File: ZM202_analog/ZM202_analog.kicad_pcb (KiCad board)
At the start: 2 copper layers, 3 parts, among them U1 2N4416, U2 TL431, U3 LM324

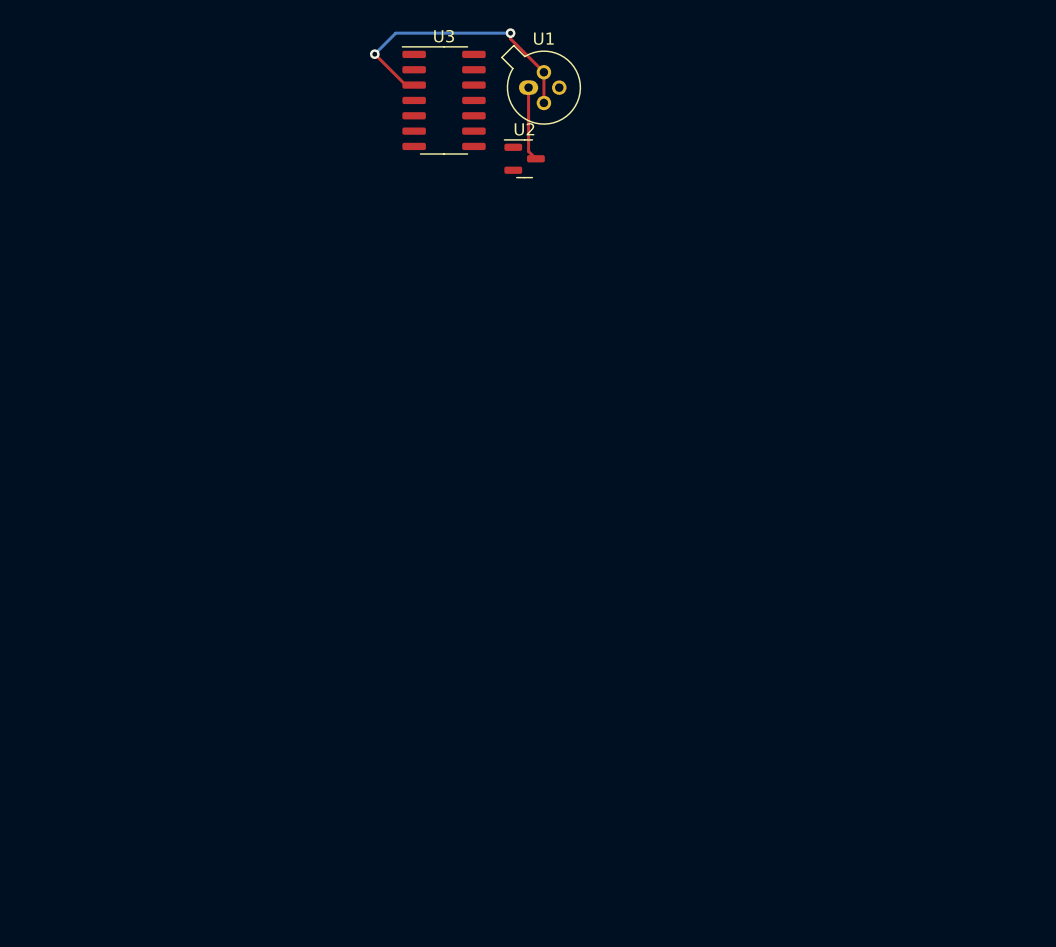
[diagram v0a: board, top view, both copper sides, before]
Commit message: Finished first version of PCB. Added some capacitors at digital ICs.
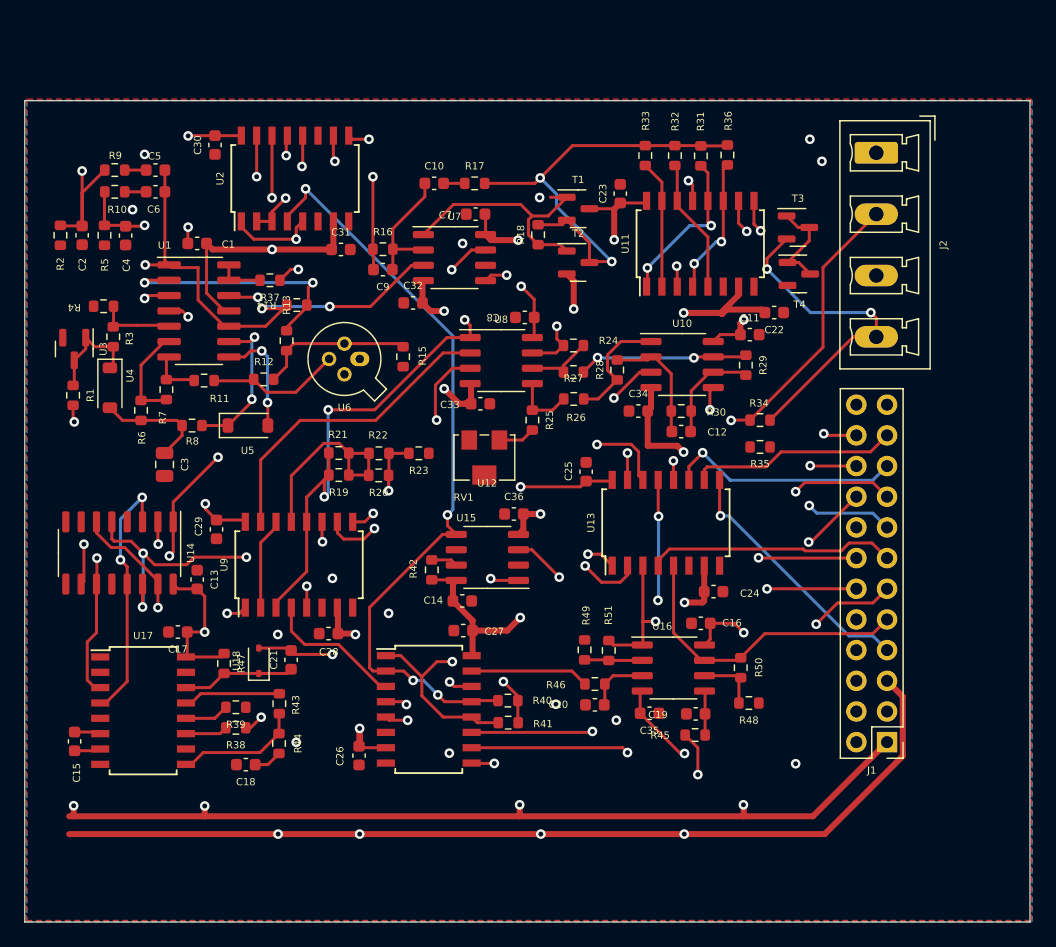
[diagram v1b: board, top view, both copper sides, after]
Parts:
- added C1: C0603_100nF_25V, Capacitor_SMD:C_0603_1608Metric, F.Cu at (37.8, 39.0)
- added C10: C0603_10nF_50V, Capacitor_SMD:C_0603_1608Metric, F.Cu at (57.5, 34.0)
- added C11: C0603_100nF_25V, Capacitor_SMD:C_0603_1608Metric, F.Cu at (83.6, 46.5)
- added C12: C0603_82nF_25V, Capacitor_SMD:C_0603_1608Metric, F.Cu at (77.9, 54.5)
- added C13: C0603_100nF_25V, Capacitor_SMD:C_0603_1608Metric, F.Cu at (37.8, 66.8)
- added C14: C0603_100nF_25V, Capacitor_SMD:C_0603_1608Metric, F.Cu at (59.8, 68.5)
- added C15: C0603_10nF_50V, Capacitor_SMD:C_0603_1608Metric, F.Cu at (27.7, 80.2)
- added C16: C0603_100nF_25V, Capacitor_SMD:C_0603_1608Metric, F.Cu at (79.5, 70.4)
- added C17: C0603_100nF_25V, Capacitor_SMD:C_0603_1608Metric, F.Cu at (36.2, 71.1)
- added C18: C0603_100nF_25V, Capacitor_SMD:C_0603_1608Metric, F.Cu at (41.9, 82.1)
- added C19: C0603_1uF_25V, Capacitor_SMD:C_0603_1608Metric, F.Cu at (79.1, 77.9)
- added C2: C0603_10nF_50V, Capacitor_SMD:C_0603_1608Metric, F.Cu at (28.3, 38.3)
- added C20: C0603_1uF_25V, Capacitor_SMD:C_0603_1608Metric, F.Cu at (70.8, 77.2)
- added C21: C0603_10nF_50V, Capacitor_SMD:C_0603_1608Metric, F.Cu at (45.6, 73.4)
- added C22: C0603_100nF_25V, Capacitor_SMD:C_0603_1608Metric, F.Cu at (85.6, 44.7)
- added C23: C0603_100nF_25V, Capacitor_SMD:C_0603_1608Metric, F.Cu at (72.8, 34.8)
- added C24: C0603_100nF_25V, Capacitor_SMD:C_0603_1608Metric, F.Cu at (80.6, 67.8)
- added C25: C0603_100nF_25V, Capacitor_SMD:C_0603_1608Metric, F.Cu at (70.0, 57.9)
- added C26: C0603_100nF_25V, Capacitor_SMD:C_0603_1608Metric, F.Cu at (51.2, 81.3)
- added C27: C0603_100nF_25V, Capacitor_SMD:C_0603_1608Metric, F.Cu at (59.9, 71.0)
- added C28: C0603_100nF_25V, Capacitor_SMD:C_0603_1608Metric, F.Cu at (48.7, 71.2)
- added C29: C0603_100nF_25V, Capacitor_SMD:C_0603_1608Metric, F.Cu at (39.4, 62.6)
- added C3: C0805_22uF_6.3V, Capacitor_SMD:C_0805_2012Metric, F.Cu at (35.1, 57.2)
- added C30: C0603_100nF_25V, Capacitor_SMD:C_0603_1608Metric, F.Cu at (39.3, 30.8)
- added C31: C0603_100nF_25V, Capacitor_SMD:C_0603_1608Metric, F.Cu at (49.7, 39.5)
- added C32: C0603_100nF_25V, Capacitor_SMD:C_0603_1608Metric, F.Cu at (55.7, 43.9)
- added C33: C0603_100nF_25V, Capacitor_SMD:C_0603_1608Metric, F.Cu at (61.3, 52.2)
- added C34: C0603_100nF_25V, Capacitor_SMD:C_0603_1608Metric, F.Cu at (74.3, 52.8)
- added C35: C0603_100nF_25V, Capacitor_SMD:C_0603_1608Metric, F.Cu at (75.3, 77.8)
- added C36: C0603_100nF_25V, Capacitor_SMD:C_0603_1608Metric, F.Cu at (64.0, 61.4)
- added C4: C0603_10nF_50V, Capacitor_SMD:C_0603_1608Metric, F.Cu at (31.9, 38.3)
- added C5: C0603_10nF_50V, Capacitor_SMD:C_0603_1608Metric, F.Cu at (34.4, 32.9)
- added C6: C0603_10nF_50V, Capacitor_SMD:C_0603_1608Metric, F.Cu at (34.4, 34.7)
- added C7: C0603_100nF_25V, Capacitor_SMD:C_0603_1608Metric, F.Cu at (60.9, 36.5)
- added C8: C0603_100nF_25V, Capacitor_SMD:C_0603_1608Metric, F.Cu at (65.0, 45.1)
- added C9: C0603_100pF_50V, Capacitor_SMD:C_0603_1608Metric, F.Cu at (53.2, 41.1)
- added J1: Conn_2x12_2.54_male, Connector_PinHeader_2.54mm:PinHeader_2x12_P2.54mm_Vertical, F.Cu at (94.9, 80.2)
- added J2: Conn_Screw_1x4_male, Connector_Phoenix_MC_HighVoltage:PhoenixContact_MCV_1,5_4-G-5.08_1x04_P5.08mm_Vertical, F.Cu at (94.0, 31.4)
- added R1: R0603_1k, Resistor_SMD:R_0603_1608Metric, F.Cu at (27.6, 51.5)
- added R10: R0603_20k, Resistor_SMD:R_0603_1608Metric, F.Cu at (31.0, 34.7)
- added R11: R0603_100k, Resistor_SMD:R_0603_1608Metric, F.Cu at (38.4, 50.3)
- added R12: R0603_100k, Resistor_SMD:R_0603_1608Metric, F.Cu at (43.3, 50.2)
- added R13: R0603_2k, Resistor_SMD:R_0603_1608Metric, F.Cu at (45.2, 47.0)
- added R14: R0603_4.75k, Resistor_SMD:R_0603_1608Metric, F.Cu at (46.1, 44.0)
- added R15: R0603_750, Resistor_SMD:R_0603_1608Metric, F.Cu at (54.9, 48.3)
- added R16: R0603_1k, Resistor_SMD:R_0603_1608Metric, F.Cu at (53.2, 39.4)
- added R17: R0603_200k, Resistor_SMD:R_0603_1608Metric, F.Cu at (60.8, 34.0)
- added R18: R0603_220, Resistor_SMD:R_0603_1608Metric, F.Cu at (66.0, 38.2)
- added R19: R0603_9.09M, Resistor_SMD:R_0603_1608Metric, F.Cu at (49.5, 58.1)
- added R2: R0603_200k, Resistor_SMD:R_0603_1608Metric, F.Cu at (26.5, 38.3)
- added R20: R0603_909k, Resistor_SMD:R_0603_1608Metric, F.Cu at (52.9, 58.1)
- added R21: R0603_90.9k, Resistor_SMD:R_0603_1608Metric, F.Cu at (49.5, 56.3)
- added R22: R0603_9.09k, Resistor_SMD:R_0603_1608Metric, F.Cu at (52.9, 56.3)
- added R23: R0603_1k, Resistor_SMD:R_0603_1608Metric, F.Cu at (56.2, 56.3)
- added R24: R0603_20k, Resistor_SMD:R_0603_1608Metric, F.Cu at (69.0, 47.4)
- added R25: R0603_18k, Resistor_SMD:R_0603_1608Metric, F.Cu at (65.6, 53.6)
- added R26: R0603_10k, Resistor_SMD:R_0603_1608Metric, F.Cu at (69.0, 51.8)
- added R27: R0603_10k, Resistor_SMD:R_0603_1608Metric, F.Cu at (69.0, 49.6)
- added R28: R0603_4.99k, Resistor_SMD:R_0603_1608Metric, F.Cu at (72.6, 49.4)
- added R29: R0603_4.99k, Resistor_SMD:R_0603_1608Metric, F.Cu at (83.2, 49.0)
- added R3: R0603_10k, Resistor_SMD:R_0603_1608Metric, F.Cu at (30.9, 46.7)
- added R30: R0603_2.49k, Resistor_SMD:R_0603_1608Metric, F.Cu at (77.9, 52.8)
- added R31: R0603_10M, Resistor_SMD:R_0603_1608Metric, F.Cu at (79.5, 31.7)
- added R32: R0603_100k, Resistor_SMD:R_0603_1608Metric, F.Cu at (77.4, 31.7)
- added R33: R0603_1k, Resistor_SMD:R_0603_1608Metric, F.Cu at (74.9, 31.7)
- added R34: R0603_1k, Resistor_SMD:R_0603_1608Metric, F.Cu at (84.4, 53.6)
- added R35: R0603_1k, Resistor_SMD:R_0603_1608Metric, F.Cu at (84.4, 55.8)
- added R36: R0603_10, Resistor_SMD:R_0603_1608Metric, F.Cu at (81.7, 31.6)
- added R37: R0603_100, Resistor_SMD:R_0603_1608Metric, F.Cu at (43.9, 42.0)
- added R38: R0603_10k, Resistor_SMD:R_0603_1608Metric, F.Cu at (41.0, 79.0)
- added R39: R0603_1M, Resistor_SMD:R_0603_1608Metric, F.Cu at (41.0, 77.3)
- added R4: R0603_1M, Resistor_SMD:R_0603_1608Metric, F.Cu at (30.1, 44.1)
- added R40: R0603_10k, Resistor_SMD:R_0603_1608Metric, F.Cu at (63.5, 76.8)
- added R41: R0603_10k, Resistor_SMD:R_0603_1608Metric, F.Cu at (63.6, 78.6)
- added R42: R0603_10k, Resistor_SMD:R_0603_1608Metric, F.Cu at (57.2, 66.0)
- added R43: R0603_330k, Resistor_SMD:R_0603_1608Metric, F.Cu at (44.6, 77.0)
- added R44: R0603_22k, Resistor_SMD:R_0603_1608Metric, F.Cu at (44.6, 80.3)
- added R45: R0603_470k, Resistor_SMD:R_0603_1608Metric, F.Cu at (79.0, 79.7)
- added R46: R0603_470k, Resistor_SMD:R_0603_1608Metric, F.Cu at (70.8, 75.4)
- added R47: R0603_10k, Resistor_SMD:R_0603_1608Metric, F.Cu at (40.0, 73.7)
- added R48: R0603_10k, Resistor_SMD:R_0603_1608Metric, F.Cu at (83.5, 77.0)
- added R49: R0603_10k, Resistor_SMD:R_0603_1608Metric, F.Cu at (69.9, 72.6)
- added R5: R0603_20k, Resistor_SMD:R_0603_1608Metric, F.Cu at (30.1, 38.3)
- added R50: R0603_15k, Resistor_SMD:R_0603_1608Metric, F.Cu at (82.8, 74.1)
- added R51: R0603_15k, Resistor_SMD:R_0603_1608Metric, F.Cu at (71.9, 72.7)
- added R6: R0603_10k, Resistor_SMD:R_0603_1608Metric, F.Cu at (33.2, 52.8)
- added R7: R0603_1M, Resistor_SMD:R_0603_1608Metric, F.Cu at (35.3, 51.0)
- added R8: R0603_2.2k, Resistor_SMD:R_0603_1608Metric, F.Cu at (37.4, 54.0)
- added R9: R0603_200k, Resistor_SMD:R_0603_1608Metric, F.Cu at (31.0, 32.9)
- added RV1: R_Potentiometer, Potentiometer_SMD:Potentiometer_Bourns_3214W_Vertical, F.Cu at (61.6, 56.7)
- added T1: BC846BLT1G, Package_TO_SOT_SMD:SOT-23, F.Cu at (69.4, 36.1)
- added T2: BC856B, Package_TO_SOT_SMD:SOT-23, F.Cu at (69.4, 40.5)
- added T3: BC846BLT1G, Package_TO_SOT_SMD:SOT-23, F.Cu at (87.6, 37.6)
- added T4: BC846BLT1G, Package_TO_SOT_SMD:SOT-23, F.Cu at (87.6, 41.5)
- added U10: TLC2272, Package_SO:SO-8_3.9x4.9mm_P1.27mm, F.Cu at (78.0, 49.0)
- added U11: CD4052B, Package_SO:SOIC-16W_5.3x10.2mm_P1.27mm, F.Cu at (79.5, 39.0)
- added U12: ~, Package_SO:SOIC-16W_5.3x10.2mm_P1.27mm, F.Cu at (57.0, 77.5)
- added U13: ~, Package_SO:SOIC-16W_5.3x10.2mm_P1.27mm, F.Cu at (76.6, 62.1)
- added U14: CD4027, Package_SO:SO-16_3.9x9.9mm_P1.27mm, F.Cu at (31.4, 64.6)
- added U15: LM393B, Package_SO:SO-8_3.9x4.9mm_P1.27mm, F.Cu at (61.9, 64.9)
- added U16: LM358B, Package_SO:SO-8_3.9x4.9mm_P1.27mm, F.Cu at (77.2, 74.1)
- added U17: ~, Package_SO:SOIC-16W_5.3x10.2mm_P1.27mm, F.Cu at (33.4, 77.6)
- added U18: BZX348, Diode_SMD:D_SOD-323, F.Cu at (42.9, 73.5)
- added U4: 1N4148, Diode_SMD:D_SOD-123, F.Cu at (30.6, 50.9)
- added U5: 1N4148, Diode_SMD:D_SOD-123, F.Cu at (42.0, 54.0)
- added U6: 2N4416, Package_TO_SOT_THT:TO-72-4, F.Cu at (51.3, 48.5)
- added U7: LM358B, Package_SO:SO-8_3.9x4.9mm_P1.27mm, F.Cu at (59.1, 40.1)
- added U8: TLC2272, Package_SO:SO-8_3.9x4.9mm_P1.27mm, F.Cu at (63.0, 48.6)
- added U9: ~, Package_SO:SOIC-16W_5.3x10.2mm_P1.27mm, F.Cu at (46.3, 65.5)
- U1: value 2N4416 -> LM324; footprint Package_TO_SOT_THT:TO-72-4 -> Package_SO:SO-14_3.9x8.65mm_P1.27mm
- U2: value TL431 -> ~; footprint Package_TO_SOT_SMD:SOT-23 -> Package_SO:SOIC-16W_5.3x10.2mm_P1.27mm
- U3: value LM324 -> TL431; footprint Package_SO:SO-14_3.9x8.65mm_P1.27mm -> Package_TO_SOT_SMD:SOT-23
- moved U3 36.9 mm to (27.6, 47.7), turned to -90 degrees
- moved U1 33.0 mm to (38.0, 44.5)
- moved U2 19.1 mm to (45.9, 33.6), turned to 90 degrees
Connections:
- U1 pad 1: Net-(U1-S) -> /AnalogCore/OSC_IN
- U1 pad 2: Net-(U1-D) -> Net-(U1A--)
- U1 pad 3: unconnected-(U1-G-Pad3) -> Net-(U1A-+)
- U1 pad 4: Net-(U1-D) -> +5V
- U2 pad 1: unconnected-(U2-K-Pad1) -> /AnalogCore/VVX
- U2 pad 2: unconnected-(U2-Ref-Pad2) -> /AnalogCore/VIX
- U2 pad 3: Net-(U1-S) -> /AnalogCore/VIX
- U3 pad 1: unconnected-(U3-Pad1) -> Net-(U3-A)
- U3 pad 2: unconnected-(U3A---Pad2) -> GND
- U3 pad 3: Net-(U1-D) -> Net-(U3-A)
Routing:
- net +5V: track 0.00 -> 332.0 mm, vias 0 -> 17
- net -5V: track 0.00 -> 310.4 mm, vias 0 -> 16
- net /AnalogCore/V_sig: track 0.00 -> 100.8 mm, vias 0 -> 5
- net /AnalogCore/GUARD: track 0.00 -> 87.5 mm, vias 0 -> 2
- net /AnalogCore/VIX: track 0.00 -> 75.4 mm, vias 0 -> 4
- net /AnalogCore/DR+: track 0.00 -> 74.8 mm, vias 0 -> 4
- net /AnalogCore/C/L: track 0.00 -> 69.2 mm, vias 0 -> 3
- net /PLL/PHI0: track 0.00 -> 67.9 mm, vias 0 -> 4
- net /AnalogCore/VSRC: track 0.00 -> 67.9 mm, vias 0 -> 3
- net /AnalogCore/VVX: track 0.00 -> 67.2 mm, vias 0 -> 5
- net /AnalogCore/VXX: track 0.00 -> 64.0 mm, vias 0 -> 4
- net /PLL/PHI90: track 0.00 -> 61.5 mm, vias 0 -> 3
- net /PLL/PHSCAL: track 0.00 -> 57.7 mm, vias 0 -> 3
- net /AnalogCore/SN+: track 0.00 -> 53.7 mm, vias 0 -> 2
- net /PLL/PHI270: track 0.00 -> 53.5 mm, vias 0 -> 4
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- added copper zone on B.Cu, net GND
- added copper zone on F.Cu, net GND
- added copper zone on In1.Cu, net GND
- added copper zone on In2.Cu, net GND
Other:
- board outline added: 83.2 x 68 mm
- copper layers 2 -> 4

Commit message: Changed board size.
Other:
- board size 83.2 x 68 mm -> 76.8 x 62.8 mm
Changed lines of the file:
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@@
     )
   )
-  (gr_rect (start 23.55 27.125) (end 106.775 95.125)
+  (gr_rect (start 23.55 27.125) (end 100.35 89.925)
     (stroke (width 0.1) (type default)) (fill none) (layer "Edge.Cuts"))
   (dimension (type aligned) (layer "F.Cu")
@@
       (pts
         (xy 23.675 27)
-        (xy 23.675 95)
-        (xy 106.9 95)
-        (xy 106.9 27)
+        (xy 24 89.8)
+        (xy 100.475 89.875)
+        (xy 100.15 27.075)
       )
     )
@@
       (pts
         (xy 23.55 27.125)
-        (xy 23.55 95.125)
-        (xy 106.775 95.125)
-        (xy 106.775 27.125)
+        (xy 23.725 90.125)
+        (xy 100.4 89.825)
+        (xy 100.25 26.675)
       )
     )
@@
       (pts
         (xy 23.575 27.125)
-        (xy 23.55 95.125)
-        (xy 106.75 95.125)
-        (xy 106.775 27.125)
+        (xy 23.675 89.9)
+        (xy 100.425 89.775)
+        (xy 100.325 27)
       )
     )
@@
       (pts
         (xy 23.725 27.125)
-        (xy 23.725 95.125)
-        (xy 106.95 95.125)
-        (xy 106.95 27.125)
+        (xy 23.7 89.775)
+        (xy 100.125 90.05)
+        (xy 100.15 27.4)
       )
     )

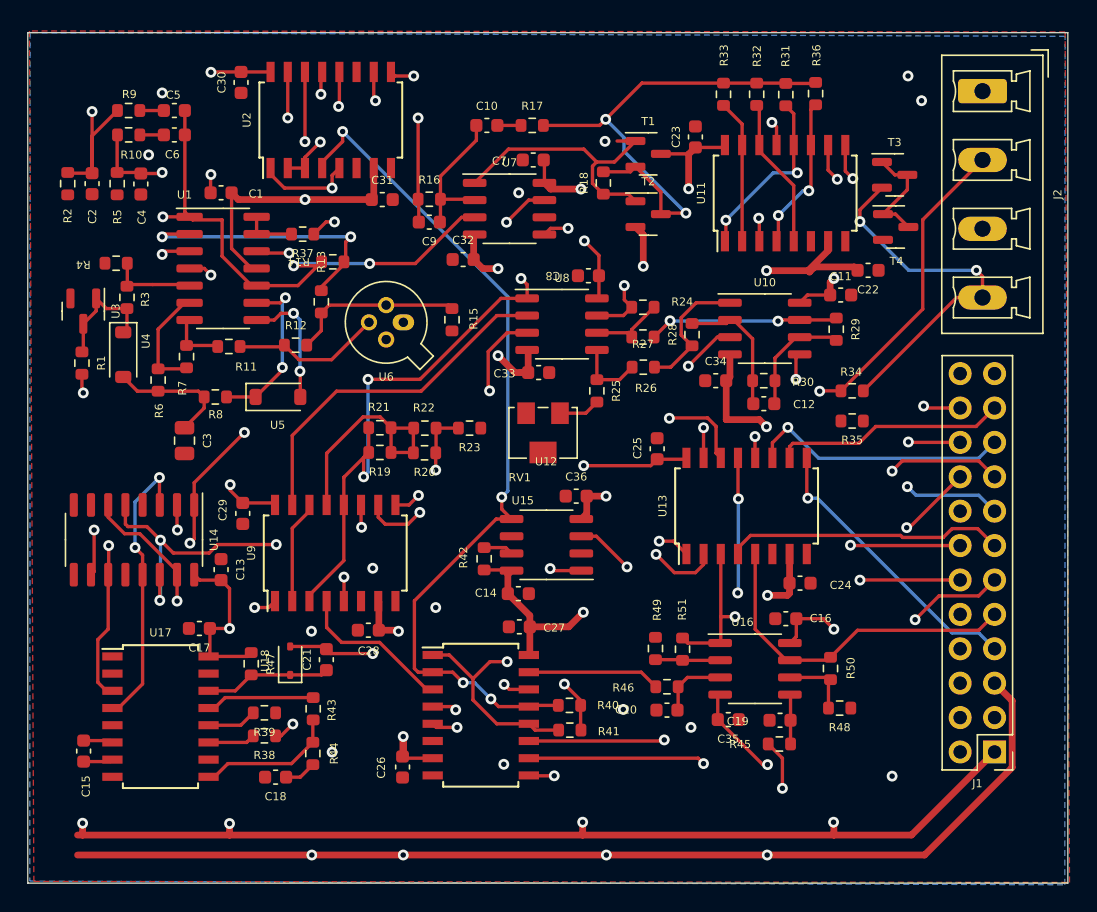
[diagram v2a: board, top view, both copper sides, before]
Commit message: Minor changes, fixed gnd-island.
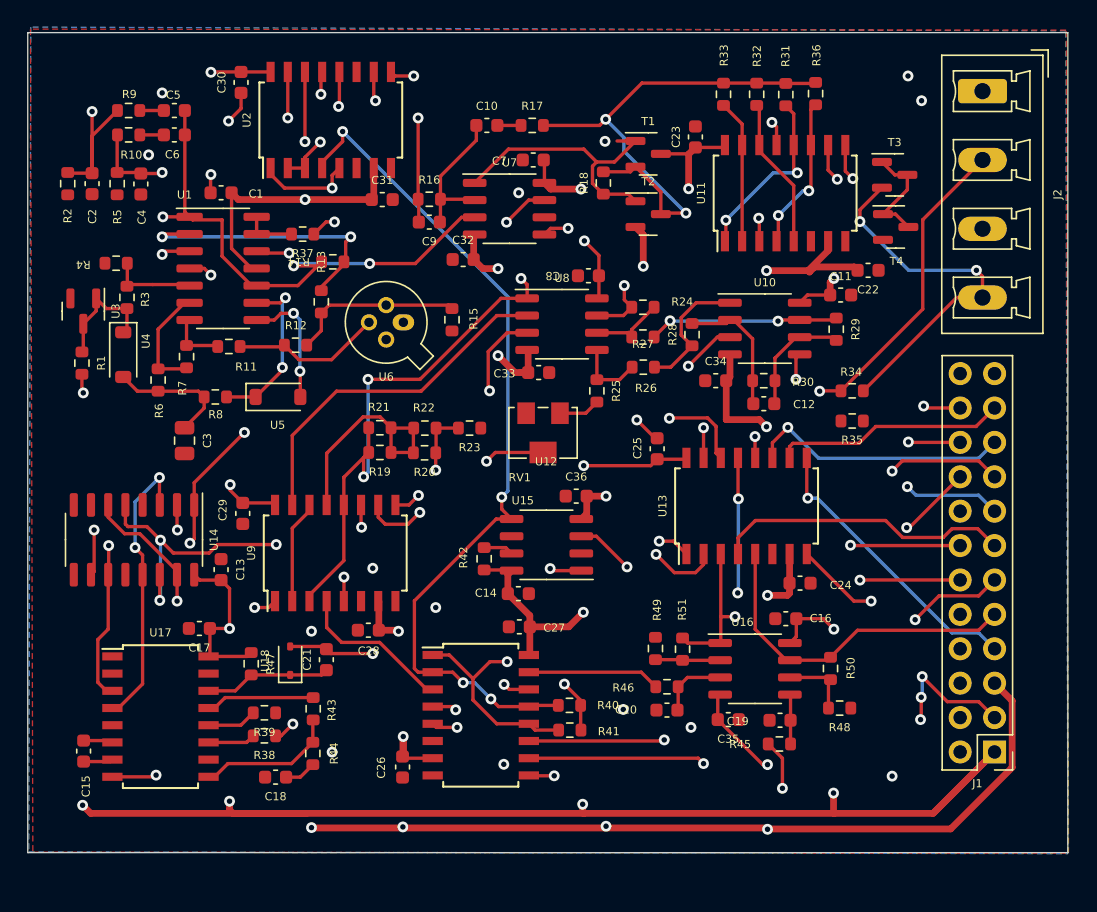
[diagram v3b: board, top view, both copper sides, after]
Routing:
- net GND: track 1.64 -> 29.9 mm, vias 1 -> 9
- net -5V: track 310.4 -> 284.4 mm
- net +5V: track 332.0 -> 336.0 mm
- net /PLL/ADC: track 20.6 -> 22.0 mm
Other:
- board size 76.8 x 62.8 mm -> 76.8 x 60.5 mm

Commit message: Outline of Raspberry-Pi added.
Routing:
- net +5V: track 336.0 -> 0.00 mm, vias 17 -> 0
- net -5V: track 284.4 -> 0.00 mm, vias 16 -> 0
- net /AnalogCore/V_sig: track 100.8 -> 0.00 mm, vias 5 -> 0
- net /AnalogCore/GUARD: track 87.5 -> 0.00 mm, vias 2 -> 0
- net /AnalogCore/VIX: track 75.4 -> 0.00 mm, vias 4 -> 0
- net /AnalogCore/DR+: track 74.8 -> 0.00 mm, vias 4 -> 0
- net /AnalogCore/C/L: track 69.2 -> 0.00 mm, vias 3 -> 0
- net /PLL/PHI0: track 67.9 -> 0.00 mm, vias 4 -> 0
- net /AnalogCore/VSRC: track 67.9 -> 0.00 mm, vias 3 -> 0
- net /AnalogCore/VVX: track 67.2 -> 0.00 mm, vias 5 -> 0
- net /AnalogCore/VXX: track 64.0 -> 0.00 mm, vias 4 -> 0
- net /PLL/PHI90: track 61.5 -> 0.00 mm, vias 3 -> 0
- net /PLL/PHSCAL: track 57.7 -> 0.00 mm, vias 3 -> 0
- net /AnalogCore/SN+: track 53.7 -> 0.00 mm, vias 2 -> 0
- net /PLL/PHI270: track 53.5 -> 0.00 mm, vias 4 -> 0
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- removed copper zone on B.Cu, net GND
- removed copper zone on F.Cu, net GND
- removed copper zone on In1.Cu, net GND
- removed copper zone on In2.Cu, net GND
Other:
- board size 76.8 x 60.5 mm -> 85 x 56 mm

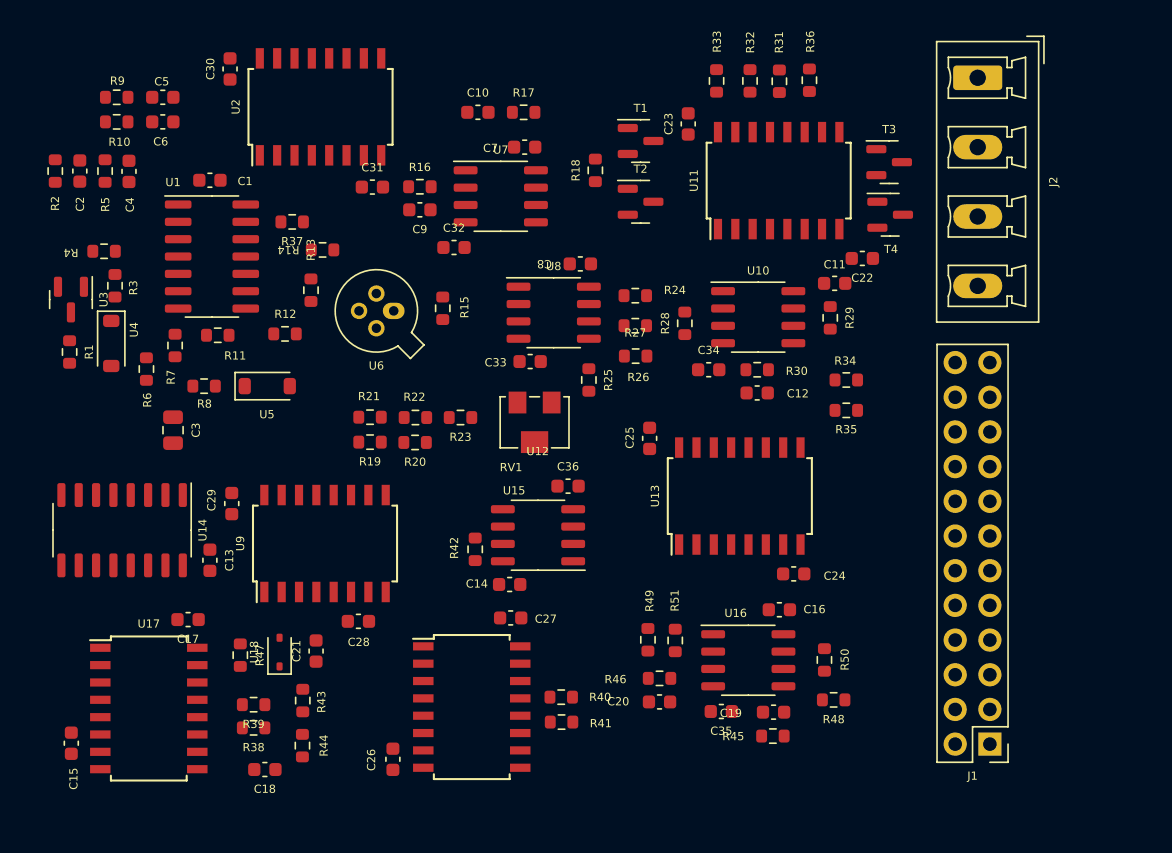
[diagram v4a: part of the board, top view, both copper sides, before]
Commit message: New part placement.
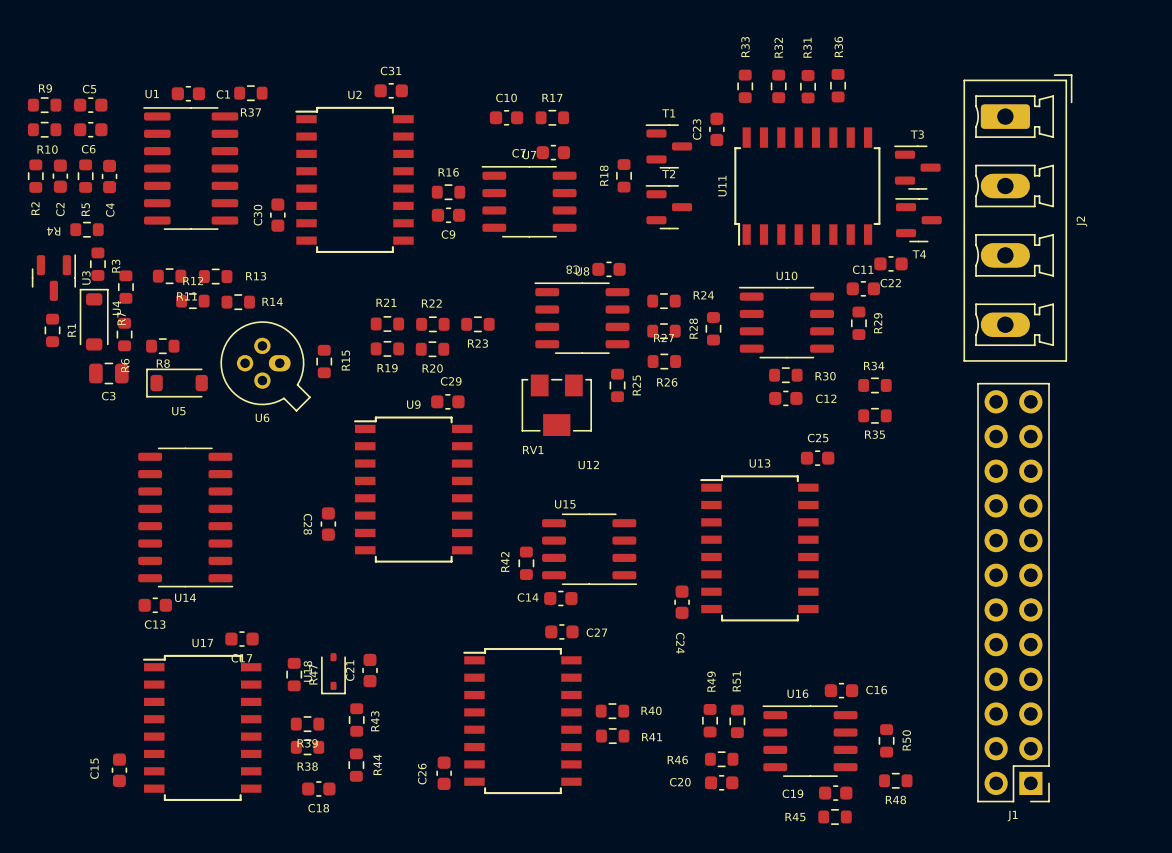
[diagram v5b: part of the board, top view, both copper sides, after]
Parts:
- removed C32, C33, C34, C35, C36: C0603_100nF_25V, Capacitor_SMD:C_0603_1608Metric
- moved C29 17.5 mm to (55.2, 55.2), turned to 180 degrees
- moved C25 12.4 mm to (82.3, 59.3), turned to 180 degrees
- moved C30 11.3 mm to (42.8, 41.5)
- moved R37 9.90 mm to (40.8, 32.6)
- moved R15 9.51 mm to (46.2, 52.2)
- moved U6 9.18 mm to (42.9, 52.4)
- moved C24 8.43 mm to (72.4, 69.8), turned to -90 degrees
- moved U9 7.60 mm to (52.8, 61.6), turned to 0 degrees
- moved R49 7.47 mm to (74.5, 78.5)
- moved U16 7.47 mm to (81.8, 80.0)
- moved C19 7.47 mm to (83.7, 83.8)
- moved C16 7.47 mm to (84.1, 76.3)
- moved C20 7.47 mm to (75.3, 83.1)
- moved R45 7.47 mm to (83.6, 85.6)
- moved R46 7.47 mm to (75.3, 81.3)
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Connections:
- C11 pad 1: GND -> -5V
- C14 pad 1: GND -> -5V
- C16 pad 1: GND -> -5V
- C30 pad 1: GND -> -5V
- C30 pad 2: +5V -> GND
- C31 pad 1: -5V -> GND
- C31 pad 2: GND -> +5V
- C7 pad 1: GND -> -5V
- C8 pad 1: GND -> -5V
